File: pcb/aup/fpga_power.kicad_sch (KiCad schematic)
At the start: 3 parts, among them U1 XC7A50T-FGG484

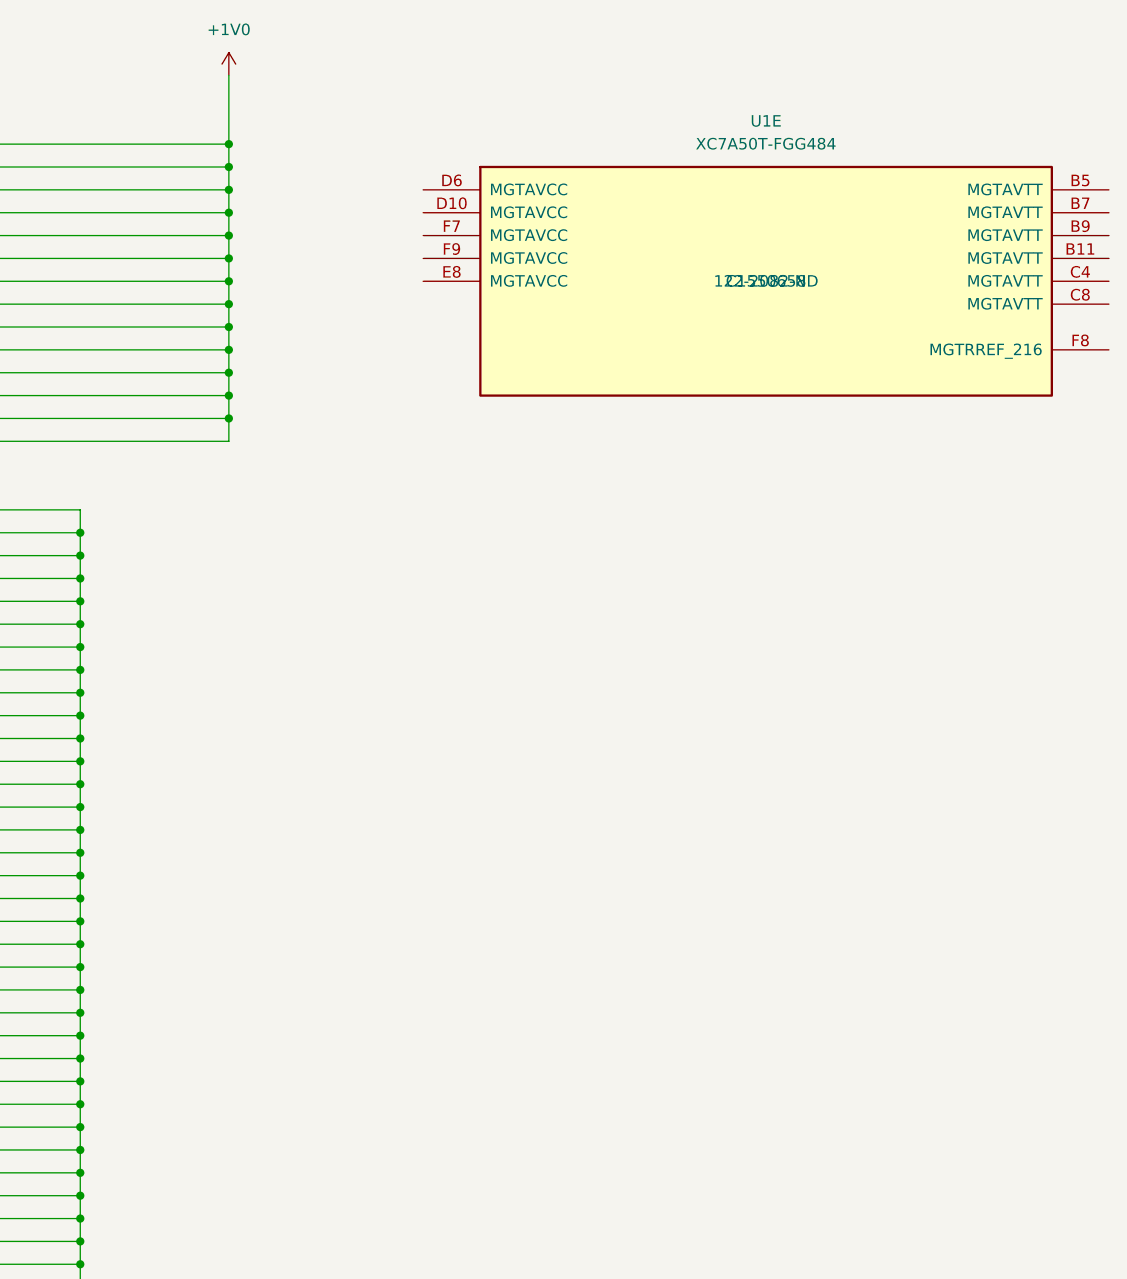
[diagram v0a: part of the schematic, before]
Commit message: Cleanup power layout
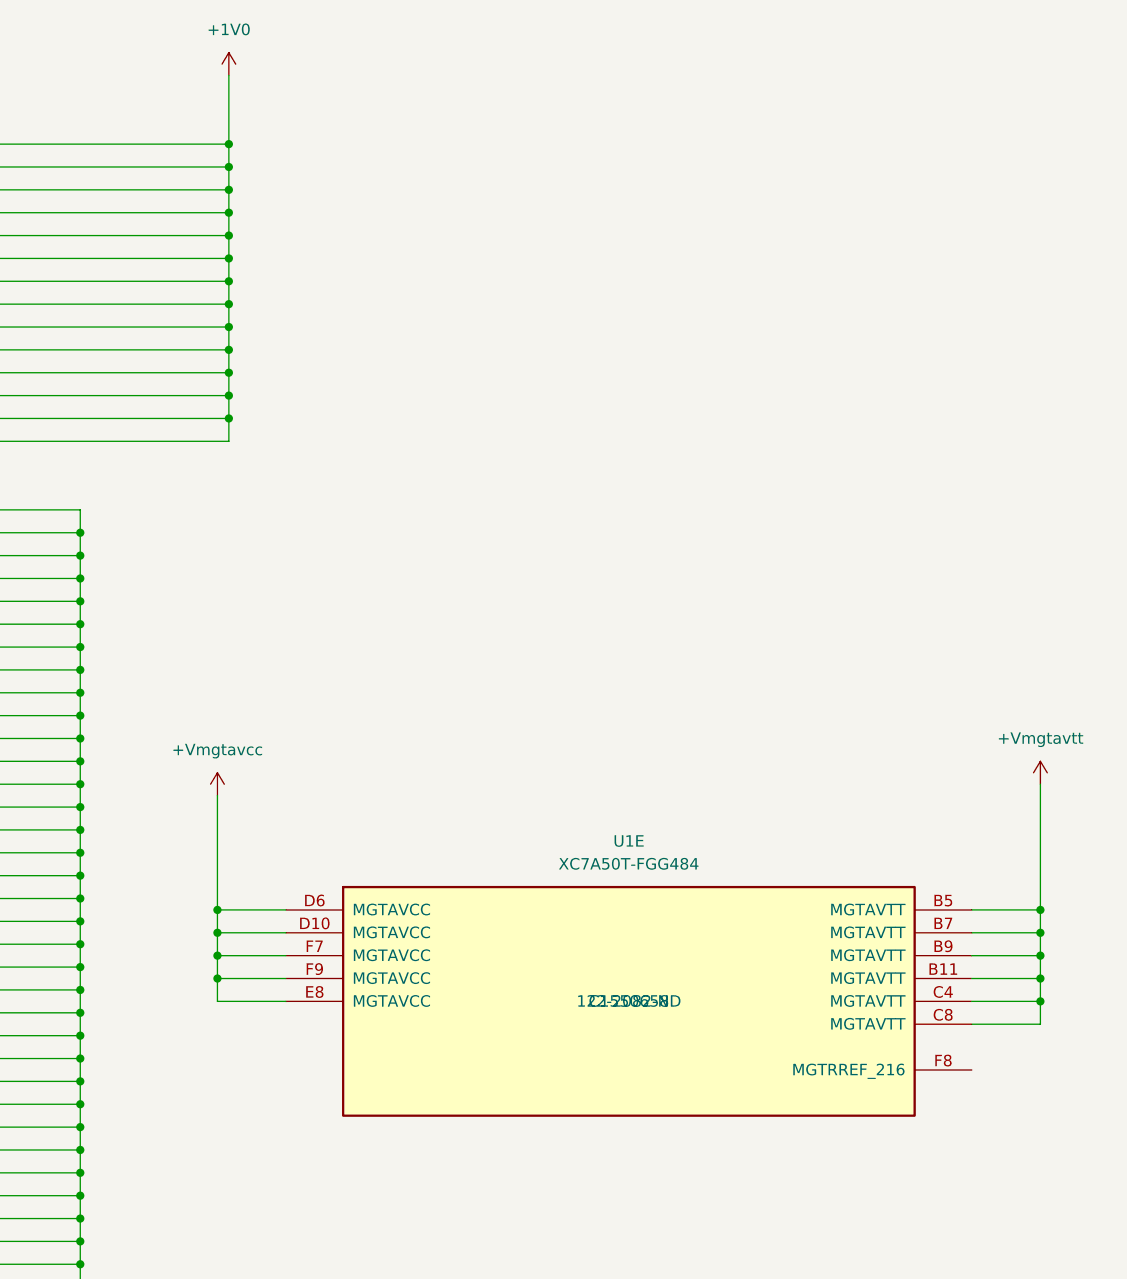
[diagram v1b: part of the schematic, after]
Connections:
- net +Vmgtavtt: now reaches U1.B11 (MGTAVTT)
- net +Vmgtavtt: now also U1.B5 (MGTAVTT), U1.B7 (MGTAVTT), U1.B9 (MGTAVTT), U1.C4 (MGTAVTT), U1.C8 (MGTAVTT)
- net +Vmgtavcc: now reaches U1.D10 (MGTAVCC)
- net +Vmgtavcc: now also U1.D6 (MGTAVCC), U1.E8 (MGTAVCC), U1.F7 (MGTAVCC), U1.F9 (MGTAVCC)
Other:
- moved on the sheet: U1E

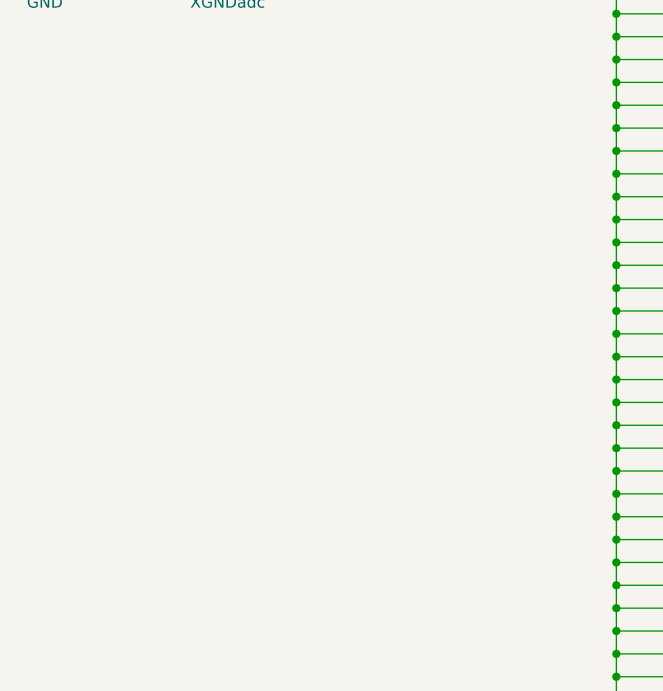
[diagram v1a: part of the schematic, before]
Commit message: All rails assigned net classes
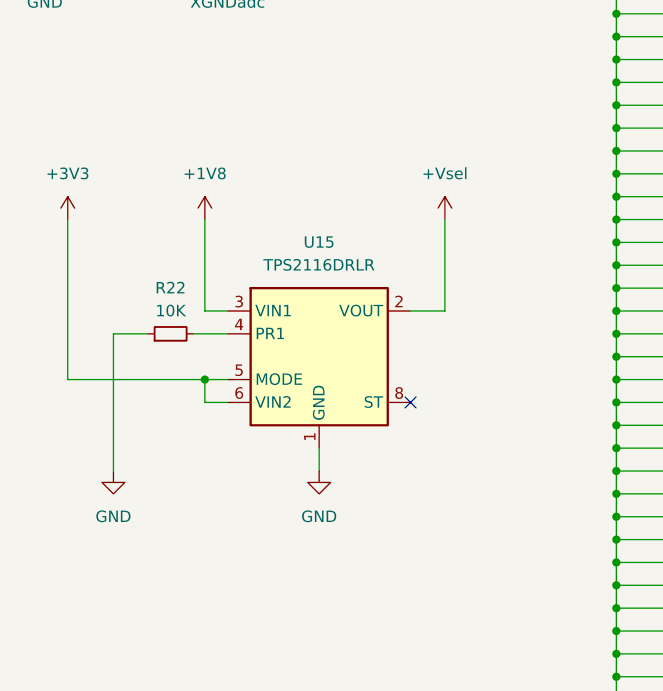
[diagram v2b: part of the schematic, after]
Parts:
- added R22: 10K, Resistor_SMD:R_0603_1608Metric, symbol !Misc:R_10K_0603
- added U15: TPS2116DRLR, Package_TO_SOT_SMD:SOT-583-8, symbol !Misc:TPS2116DRLR
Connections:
- net +1V8: now also U15.3 (VIN1)
- net GND: now also R22.1, U15.1 (GND)
- new net: R22.2, U15.4 (PR1)
- new net +3V3: U15.5 (MODE), U15.6 (VIN2)
- new net +Vsel: U15.2 (VOUT), U15.7 (VOUT)
- no-connect marks 0 -> 1
